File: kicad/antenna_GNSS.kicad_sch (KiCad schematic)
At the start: 1 part, among them J8 SMA_CONNECTOR

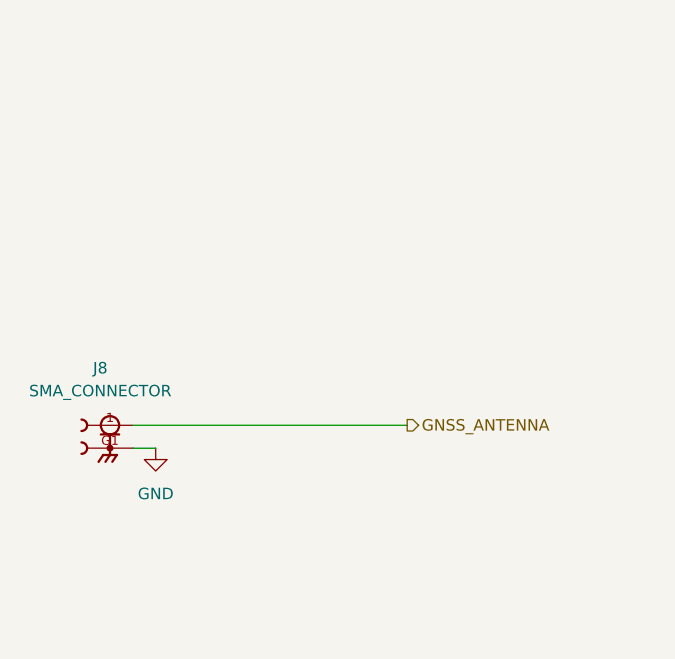
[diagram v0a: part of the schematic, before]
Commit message: feat: update GNSS circuit
Signed-off-by: Bobo Bäck Engström <bobo@id8-engineering.io>
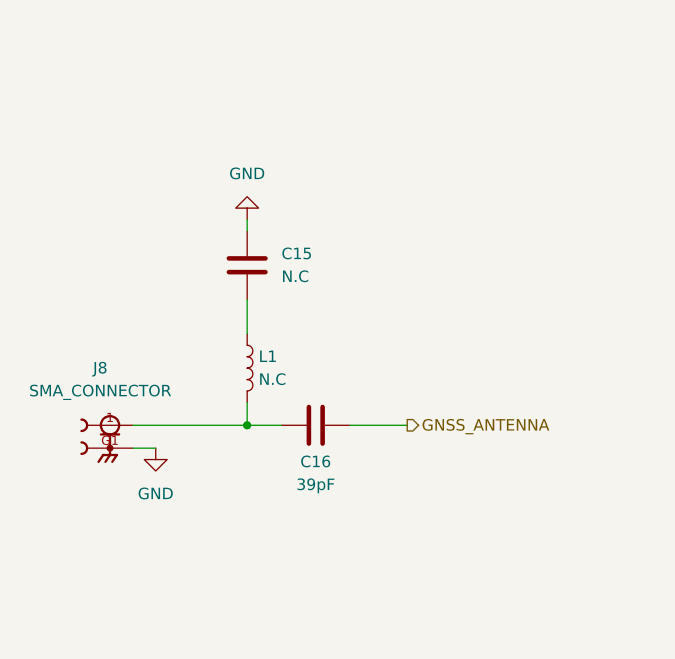
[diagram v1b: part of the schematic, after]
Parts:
- added C15: N.C, seven-lib:C_1812_4532Metric, symbol seven_lib:C
- added C16: 39pF, seven-lib:C_1812_4532Metric, symbol seven_lib:C
- added L1: N.C, seven-lib:L_1008_2520Metric, symbol seven_lib:L
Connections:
- net GND: now also C15.1
- net GNSS_ANTENNA: now also C16.2; no longer J8.1
- new net: C16.1, J8.1, L1.2
- new net: C15.2, L1.1

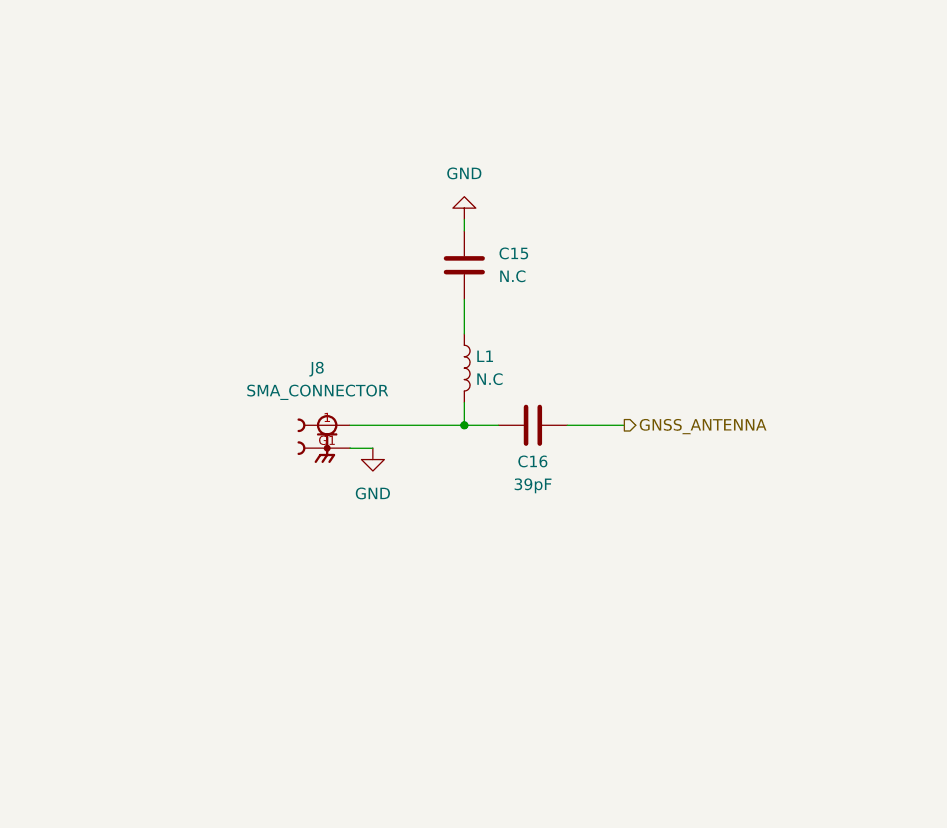
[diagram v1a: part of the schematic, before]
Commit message: fix: change GNSS circuit to follow nRF9151DK SMA connectors
Signed-off-by: Bobo Bäck Engström <bobo@id8-engineering.io>
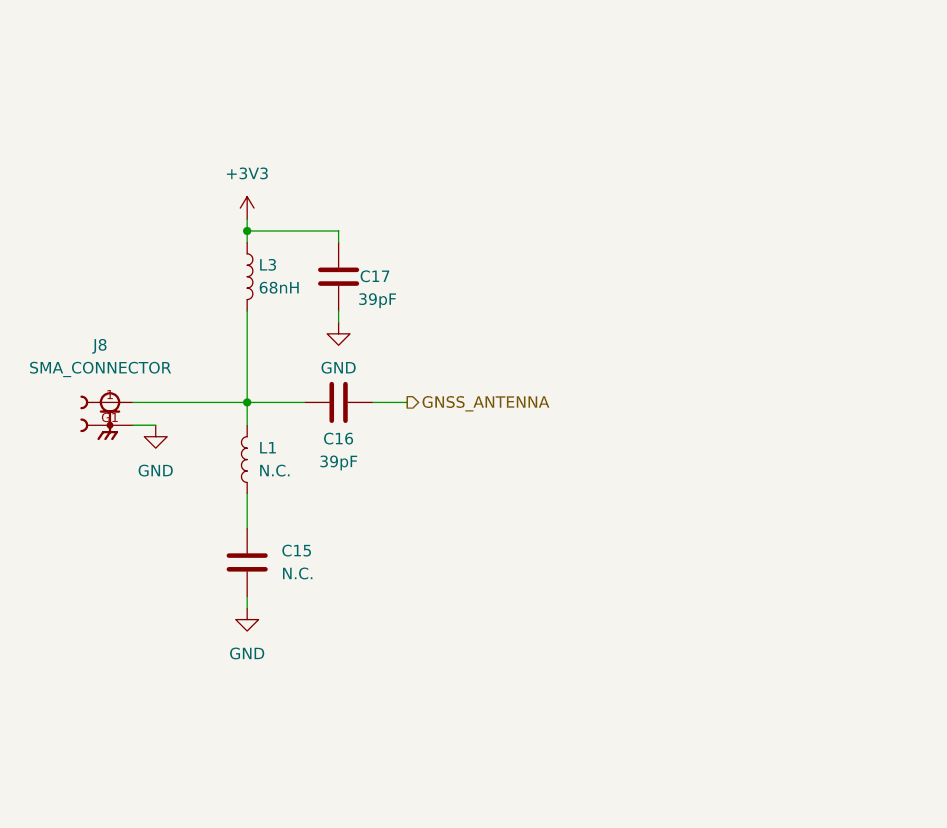
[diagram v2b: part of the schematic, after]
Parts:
- added C17: 39pF, seven-lib:C_1812_4532Metric, symbol seven_lib:C
- added L3: 68nH, seven-lib:L_1008_2520Metric, symbol seven_lib:L
- C15, L1: value N.C -> N.C.
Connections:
- net GND: now also C17.1
- net at C16.1, J8.1, L1.2: now also L3.2
- new net +3V3: C17.2, L3.1
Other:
- moved on the sheet: C15, C16, J8, L1

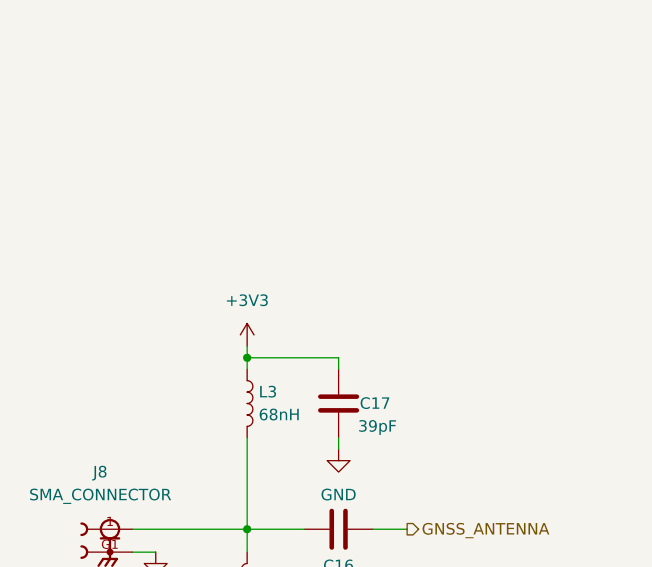
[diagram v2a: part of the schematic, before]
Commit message: feat: remake power management and use the same as the reference DK
Signed-off-by: Bobo Bäck Engström <bobo@id8-engineering.io>
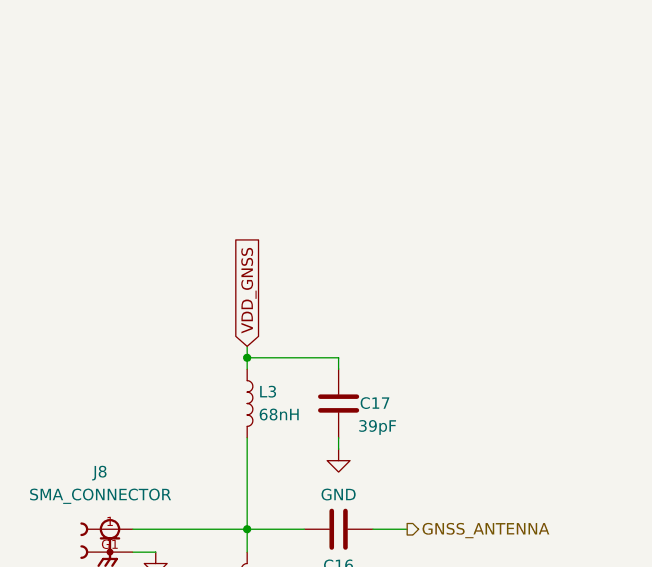
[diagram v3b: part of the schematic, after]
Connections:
- net +3V3 renamed VDD_GNSS
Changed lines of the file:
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@@
+		)
+	)
+	(global_label "VDD_GNSS"
+		(shape input)
+		(at 85.09 69.85 90)
+		(fields_autoplaced yes)
+		(effects
+			(font
+				(size 1.27 1.27)
+			)
+			(justify left)
+		)
+		(property "Intersheetrefs" "${INTERSHEET_REFS}"
+			(at 85.09 57.2491 90)
+			(effects
+				(font
+					(size 1.27 1.27)
+				)
+				(justify left)
+				(hide yes)
+			)
 		)
 	)
@@
 					(unit 1)
 				)
-			)
-		)
-	)
-	(symbol
-		(lib_id "seven_lib:+3V3")
-		(at 85.09 69.85 0)
-		(unit 1)
-		(exclude_from_sim no)
-		(in_bom yes)
-		(on_board yes)
-		(dnp no)
-		(fields_autoplaced yes)
-		(property "Reference" "#PWR022"
-			(at 85.09 73.66 0)
-			(effects
-				(font
-					(size 1.27 1.27)
-				)
-				(hide yes)
-			)
-		)
-		(property "Value" "+3V3"
-			(at 85.09 64.77 0)
-			(effects
-				(font
-					(size 1.27 1.27)
-				)
-			)
-		)
-		(property "Footprint" ""
-			(at 85.09 69.85 0)
-			(effects
-				(font
-					(size 1.27 1.27)
-				)
-				(hide yes)
-			)
-		)
-		(property "Datasheet" ""
-			(at 85.09 69.85 0)
-			(effects
-				(font
-					(size 1.27 1.27)
-				)
-				(hide yes)
-			)
-		)
-		(property "Description" "Power symbol creates a global label with name \"+3V3\""
-			(at 85.09 69.85 0)
-			(effects
-				(font
-					(size 1.27 1.27)
-				)
-				(hide yes)
-			)
-		)
-		(pin "1"
-		)
-		(instances
-			(project ""
-				(path "/8e3cc843-5797-49f3-8b3a-1c11450ccd1e/e0d7d36a-9918-47c0-a519-1a389fc09cdf"
-					(reference "#PWR022")
-					(unit 1)
-				)

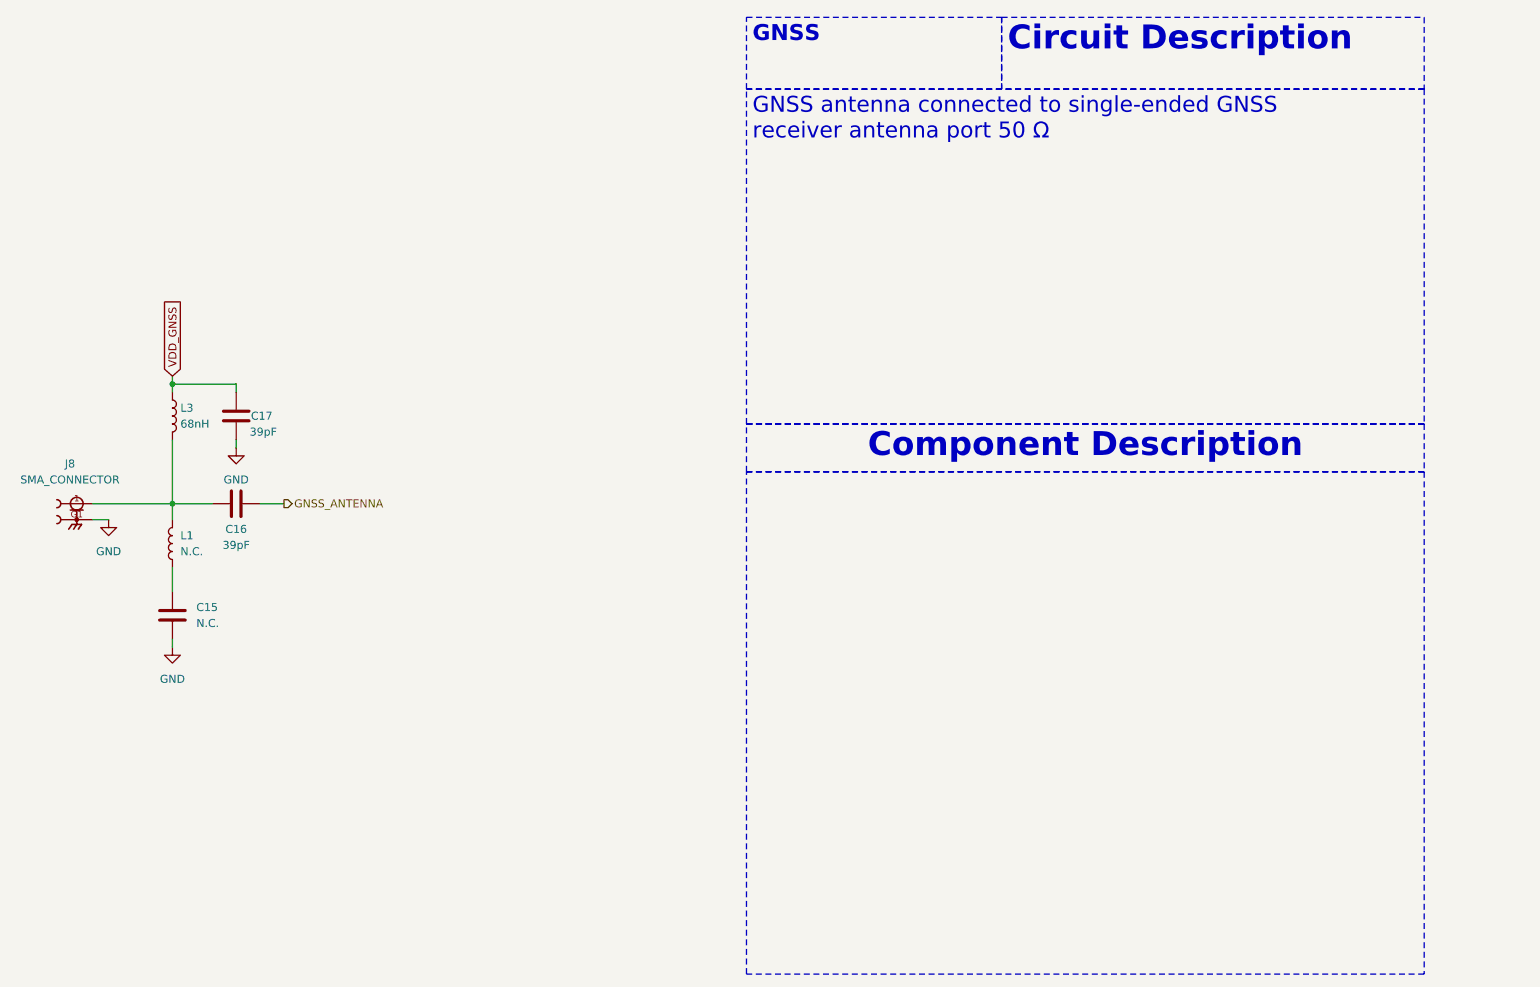
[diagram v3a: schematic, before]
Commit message: docs: update documentation to be more accurate
Signed-off-by: Bobo Bäck Engström <bobo@id8-engineering.io>
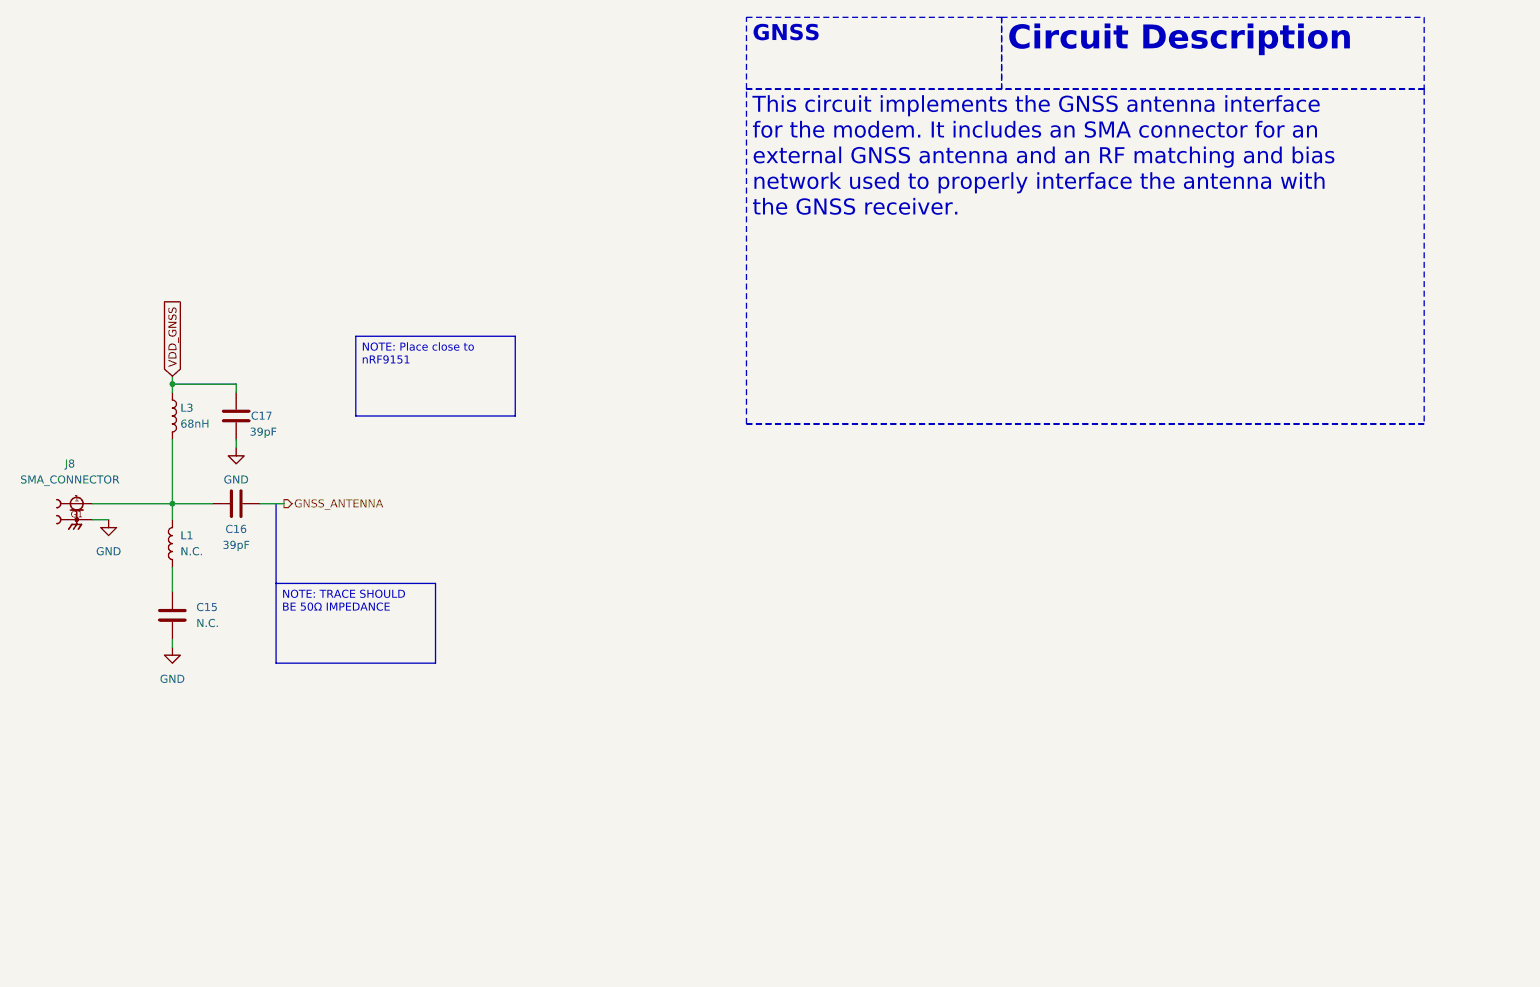
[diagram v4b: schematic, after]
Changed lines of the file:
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@@
 		)
 	)
-	(text_box "GNSS antenna connected to single-ended GNSS receiver antenna port 50 Ω"
+	(text_box "This circuit implements the GNSS antenna interface for the modem. It includes an SMA connector for an external GNSS antenna and an RF matching and bias network used to properly interface the antenna with the GNSS receiver."
 		(exclude_from_sim no)
 		(at 176.53 24.13 0)
@@
 		)
 	)
-	(text_box "\n"
-		(exclude_from_sim no)
-		(at 176.53 85.09 0)
-		(size 107.95 80.01)
-		(margins 0.9525 0.9525 0.9525 0.9525)
-		(stroke
-			(width 0)
-			(type dash)
-		)
-		(fill
-			(type none)
-		)
-		(effects
-			(font
-				(size 2.54 2.54)
-			)
-			(justify left top)
-		)
-	)
-	(text_box "Component Description\n"
-		(exclude_from_sim no)
-		(at 176.53 77.47 0)
-		(size 107.95 7.62)
-		(margins 0.9525 0.9525 0.9525 0.9525)
-		(stroke
-			(width 0)
-			(type dash)
-		)
-		(fill
-			(type none)
-		)
-		(effects
-			(font
-				(size 3.81 3.81)
-				(thickness 0.762)
-				(bold yes)
-			)
-			(justify top)
+	(text_box "NOTE: TRACE SHOULD BE 50Ω IMPEDANCE\n"
+		(exclude_from_sim no)
+		(at 101.6 102.87 0)
+		(size 25.4 12.7)
+		(margins 0.9525 0.9525 0.9525 0.9525)
+		(stroke
+			(width 0)
+			(type solid)
+			(color 255 0 0 1)
+		)
+		(fill
+			(type color)
+			(color 255 67 78 1)
+		)
+		(effects
+			(font
+				(size 1.27 1.27)
+				(color 0 0 0 1)
+			)
+			(justify left top)
+		)
+	)
+	(text_box "NOTE: Place close to nRF9151"
+		(exclude_from_sim no)
+		(at 114.3 63.5 0)
+		(size 25.4 12.7)
+		(margins 0.9525 0.9525 0.9525 0.9525)
+		(stroke
+			(width 0)
+			(type solid)
+			(color 255 0 0 1)
+		)
+		(fill
+			(type color)
+			(color 255 67 78 1)
+		)
+		(effects
+			(font
+				(size 1.27 1.27)
+				(color 0 0 0 1)
+			)
+			(justify left top)
 		)
 	)
@@
 		)
 		(stroke
+			(width 0)
+			(type default)
+		)
+	)
+	(polyline
+		(pts
+			(xy 101.6 90.17) (xy 101.6 102.87)
+		)
+		(stroke

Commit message: fix: change C fp to smaller one.
Signed-off-by: Bobo Bäck Engström <bobo@id8-engineering.io>
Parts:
- C15, C16, C17: footprint seven-lib:C_1812_4532Metric -> seven-lib:C_0402_1005Metric
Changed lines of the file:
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@@
 			)
 		)
-		(property "Footprint" "seven-lib:C_1812_4532Metric"
+		(property "Footprint" "seven-lib:C_0402_1005Metric"
 			(at 94.2848 72.39 0)
 			(effects
@@
 			)
 		)
-		(property "Footprint" "seven-lib:C_1812_4532Metric"
+		(property "Footprint" "seven-lib:C_0402_1005Metric"
 			(at 99.06 89.2048 0)
 			(effects
@@
 			)
 		)
-		(property "Footprint" "seven-lib:C_1812_4532Metric"
+		(property "Footprint" "seven-lib:C_0402_1005Metric"
 			(at 84.1248 104.14 0)
 			(effects

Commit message: fix: change R fp to a smaller one
Signed-off-by: Bobo Bäck Engström <bobo@id8-engineering.io>
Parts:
- L1, L3: footprint seven-lib:L_1008_2520Metric -> seven-lib:L_0603_1608Metric
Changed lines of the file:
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@@
 			)
 		)
-		(property "Footprint" "seven-lib:L_1008_2520Metric"
+		(property "Footprint" "seven-lib:L_0603_1608Metric"
 			(at 85.09 96.52 0)
 			(effects
@@
 			)
 		)
-		(property "Footprint" "seven-lib:L_1008_2520Metric"
+		(property "Footprint" "seven-lib:L_0603_1608Metric"
 			(at 85.09 76.2 0)
 			(effects

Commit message: fix: changes made according to review meeting
Signed-off-by: Bobo Bäck Engström <bobo@id8-engineering.io>
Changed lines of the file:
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@@
 		)
 	)
-	(text_box "NOTE: TRACE SHOULD BE 50Ω IMPEDANCE\n"
+	(text_box "Note: The trace should have a characteristic impedance of 50 Ω."
 		(exclude_from_sim no)
 		(at 101.6 102.87 0)
-		(size 25.4 12.7)
-		(margins 0.9525 0.9525 0.9525 0.9525)
-		(stroke
-			(width 0)
-			(type solid)
-			(color 255 0 0 1)
-		)
-		(fill
-			(type color)
-			(color 255 67 78 1)
-		)
-		(effects
-			(font
-				(size 1.27 1.27)
-				(color 0 0 0 1)
-			)
-			(justify left top)
-		)
-	)
-	(text_box "NOTE: Place close to nRF9151"
-		(exclude_from_sim no)
-		(at 114.3 63.5 0)
 		(size 25.4 12.7)
 		(margins 0.9525 0.9525 0.9525 0.9525)
@@
 			)
 			(justify left top)
+		)
+	)
+	(text_box "Note: Place SMA close to the nRF9151."
+		(exclude_from_sim no)
+		(at 134.62 64.77 0)
+		(size 25.4 12.7)
+		(margins 0.9525 0.9525 0.9525 0.9525)
+		(stroke
+			(width 0)
+			(type solid)
+			(color 255 0 0 1)
+		)
+		(fill
+			(type color)
+			(color 255 67 78 1)
+		)
+		(effects
+			(font
+				(size 1.27 1.27)
+				(color 0 0 0 1)
+			)
+			(justify left top)

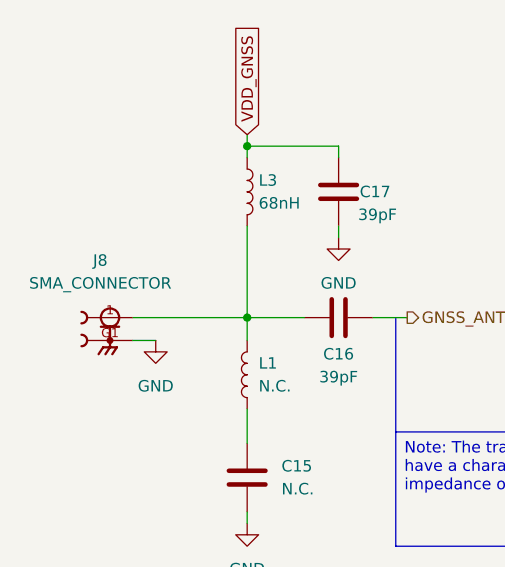
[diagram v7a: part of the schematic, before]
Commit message: feat(PCB): set component-placement example on PCB
This pr will fail due to DRC, skip this and lets have a conversation
about the placement only

Signed-off-by: Bobo Bäck Engström <bobo@id8-engineering.io>
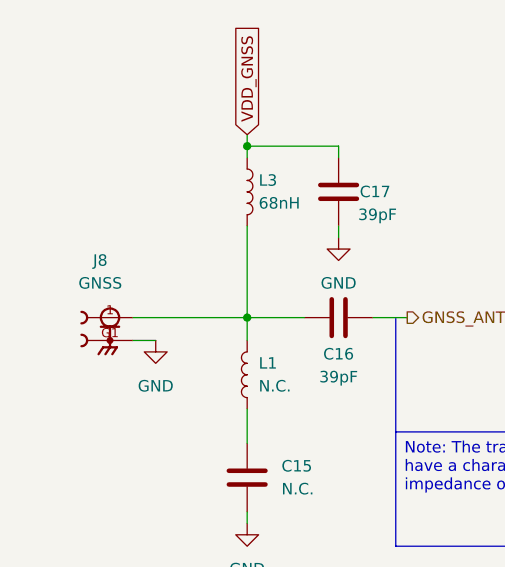
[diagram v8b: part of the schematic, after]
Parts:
- C16, C17: MPN (none) -> GRM1555C1H390JA01D
- J8: value SMA_CONNECTOR -> GNSS; Availability In Stock -> (none); Check_prices https://www.snapeda.com/parts/SMA%20CONNECTOR/LPRS/view-par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 -> (none); Description_1 RF Coaxial Straight SMA Connector -> (none); MANUFACTURER LPRS -> (none); MAXIMUM_PACKAGE_HEIGHT 8.3 mm -> (none); MF LPRS -> (none); MP SMA CONNECTOR -> (none); MPN (none) -> 2081679-1; PARTREV 1.3 -> (none); Package None -> (none); Price None -> (none); Purchase-URL https://www.snapeda.com/api/url_track_click_mouser/?unipart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 -> (none); STANDARD Manufacturer Recommendations -> (none); SnapEDA_Link https://www.snapeda.com/parts/SMA%20CONNECTOR/LPRS/view-par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 -> (none)
- L3: MPN (none) -> LQW18AN68NG80D
